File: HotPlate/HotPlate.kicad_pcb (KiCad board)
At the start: 2 copper layers, 64 x 39 mm, 61 parts, among them J1 USB_C_Receptacle_USB2.0_14P, J2 Heater, Q1 STU417S, Q4 MS50N06, SW1 RESET, SW2 BOOT, SW3 BTN0, SW4 BTN1, SW5 BTN2, SW6 BTN3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

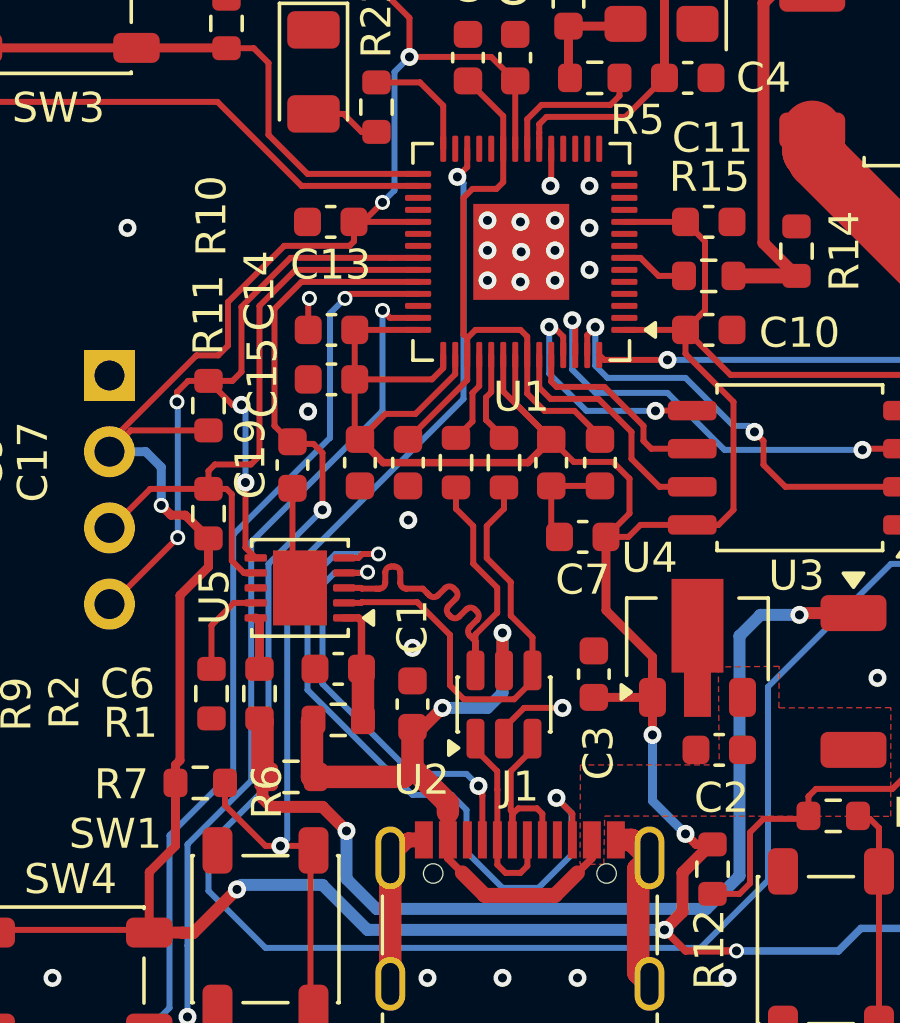
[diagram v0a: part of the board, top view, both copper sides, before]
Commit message: Remove the USBLC6 since i forgot that im using 20v and not 5v
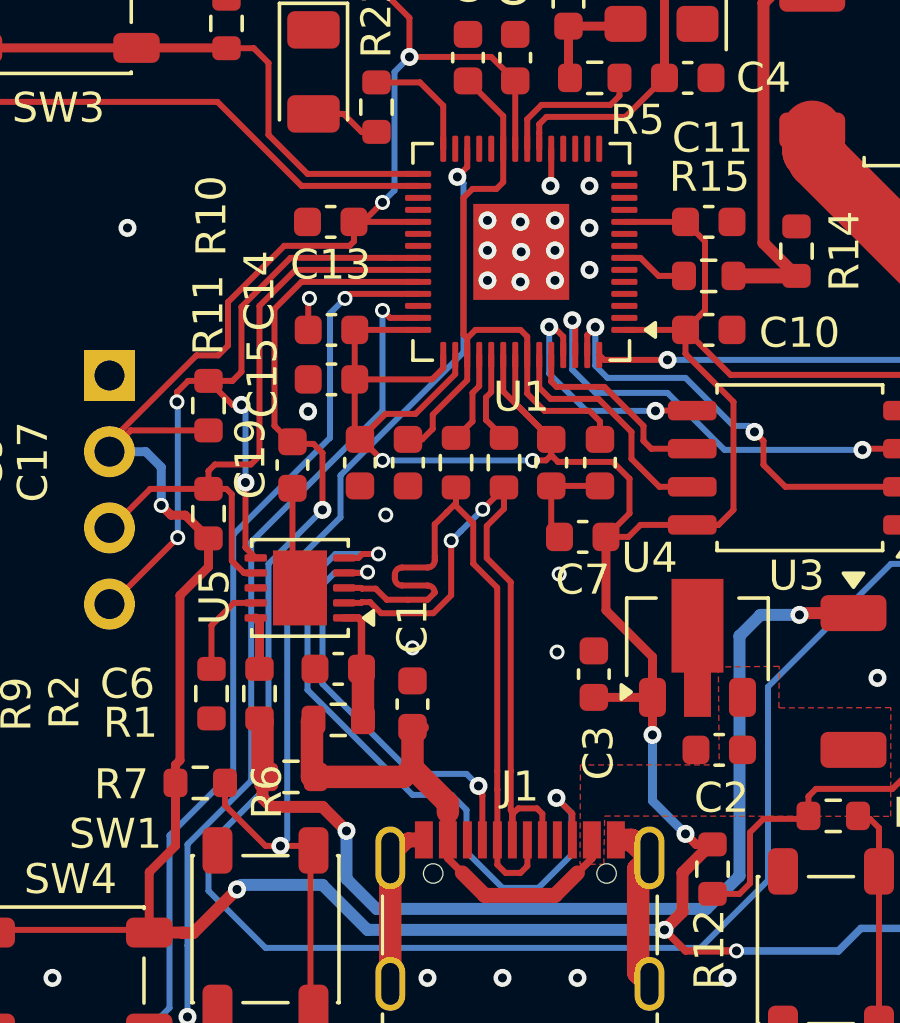
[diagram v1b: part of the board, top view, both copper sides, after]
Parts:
- removed U2: USBLC6-2SC6, Package_TO_SOT_SMD:SOT-23-6
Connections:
- J1 pad A6: /D+ -> /DOut+
- J1 pad A7: /D- -> /DOut-
- J1 pad B6: /D+ -> /DOut+
- J1 pad B7: /D- -> /DOut-
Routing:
- net /DOut-: track 17.2 -> 24.0 mm
- net /DOut+: track 17.0 -> 23.7 mm, vias 0 -> 2
- net /D-: track 6.58 -> 0.00 mm
- net /D+: track 6.58 -> 0.00 mm
- net /VBUS: track 23.4 -> 17.0 mm, vias 2 -> 0
- net GND: track 23.6 -> 20.6 mm, vias 60 -> 61
- net +1V1: track 21.5 -> 22.1 mm
- net +3V3: vias 9 -> 11
